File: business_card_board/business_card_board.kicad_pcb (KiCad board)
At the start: 2 copper layers, 85 x 54 mm, 23 parts, among them J1 PICKit3_Programmer, U1 PIC12F1822

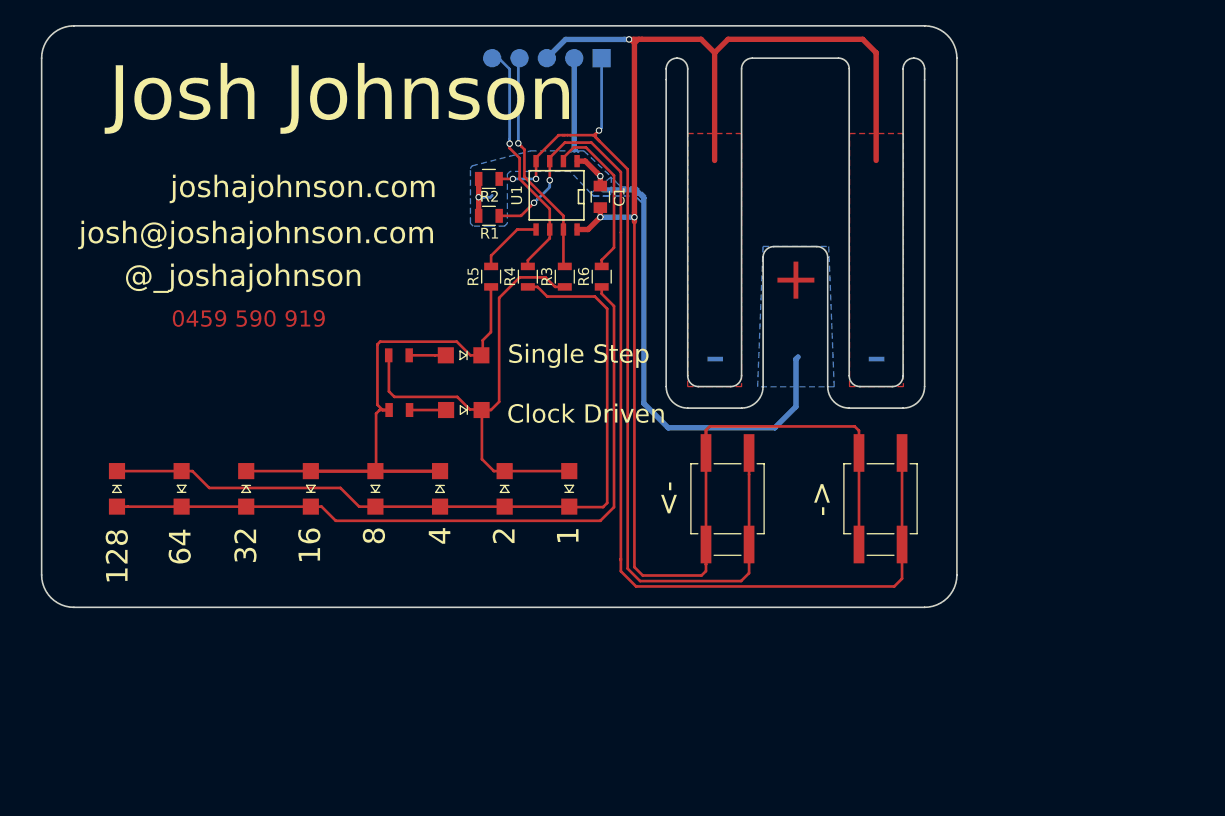
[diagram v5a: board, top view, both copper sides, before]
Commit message: board now at v1.1, improved mechanical layout + small routing changes
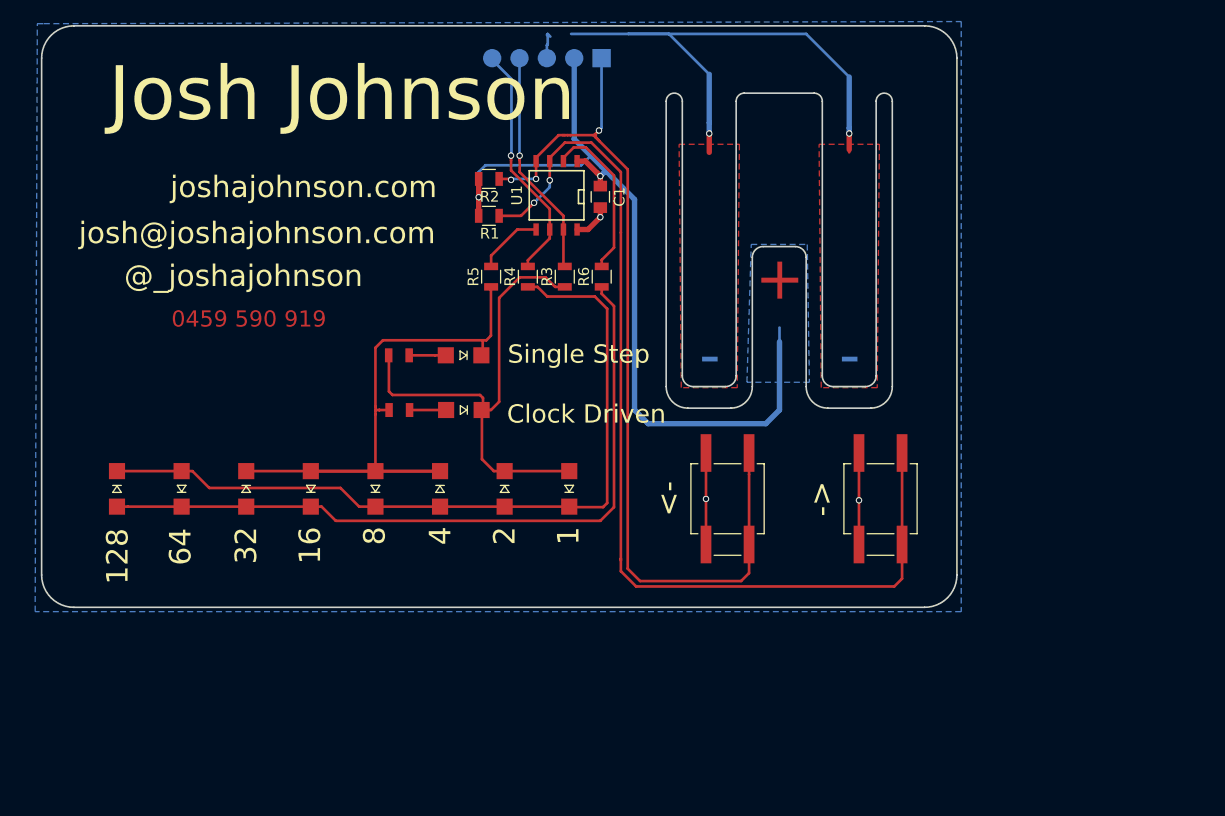
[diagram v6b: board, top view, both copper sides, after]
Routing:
- net GND: track 161.0 -> 75.0 mm, vias 3 -> 5
- net VCC: track 63.4 -> 85.0 mm
- net Net-(D1-Pad2): track 44.6 -> 45.3 mm
- net Net-(D3-Pad1): track 61.0 -> 60.4 mm
- added copper zone on B.Cu, net GND
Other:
- outline, holes or cut-outs redrawn

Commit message: more routing improvements
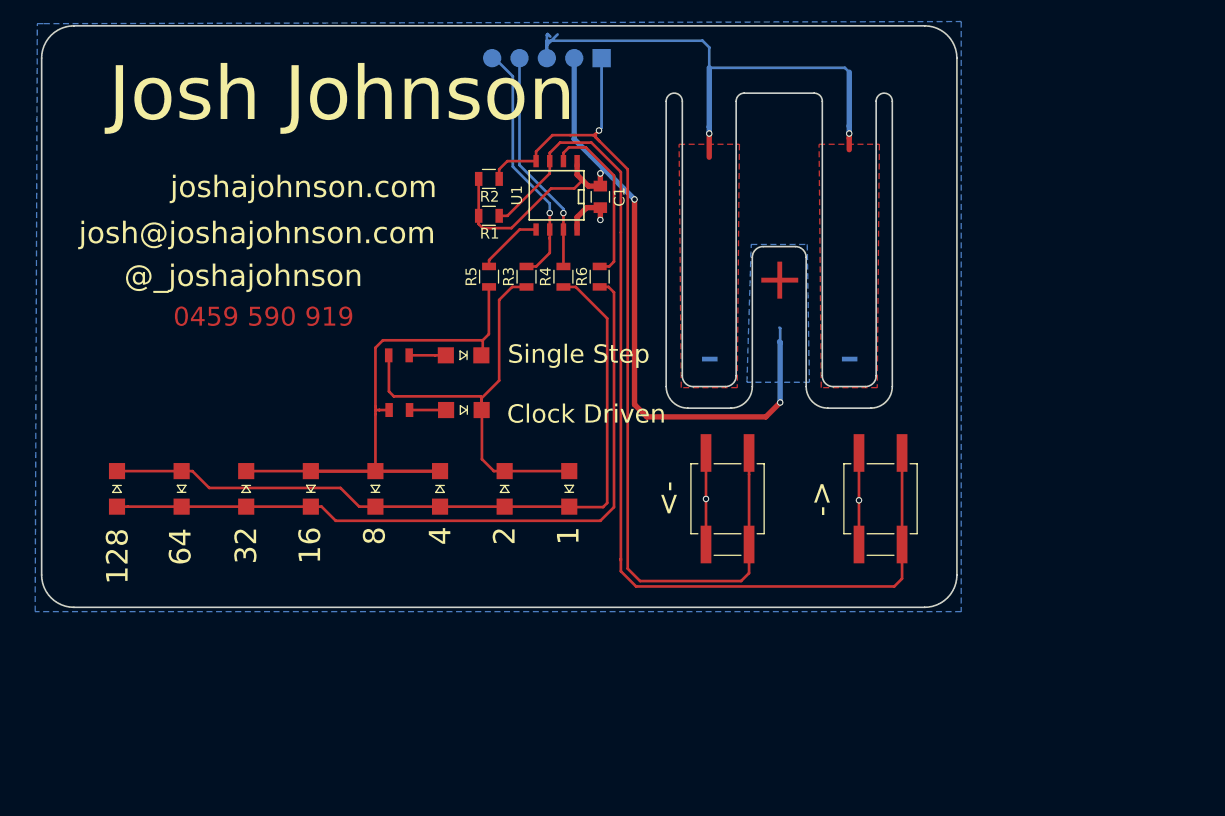
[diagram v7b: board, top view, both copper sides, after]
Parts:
- moved R3 3.56 mm to (105.0, 78.3)
- moved R4 3.30 mm to (108.5, 78.3)
- moved R5 0.19 mm to (101.6, 78.3)
- moved R6 0.19 mm to (111.8, 78.3)
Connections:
- R3 pad 2: ICSPDAT -> ICSPCLK
- R4 pad 2: ICSPCLK -> ICSPDAT
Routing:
- net Net-(D1-Pad2): track 45.3 -> 40.3 mm
- net Net-(D1-Pad1): track 73.3 -> 69.5 mm
- net VCC: track 85.0 -> 83.5 mm, vias 2 -> 3
- net RA5: track 15.4 -> 16.3 mm
- net ICSPCLK: track 22.4 -> 23.1 mm
- net Net-(D5-Pad1): track 68.4 -> 69.0 mm
- net Net-(R1-Pad2): track 92.7 -> 92.2 mm, vias 2 -> 0
- net VPP/~MCLR: track 85.0 -> 84.9 mm, vias 3 -> 1

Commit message: more routing changes
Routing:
- net VCC: track 83.5 -> 76.5 mm
- net GND: track 75.3 -> 71.2 mm
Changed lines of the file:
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@@
     (links 45)
     (no_connects 0)
-    (area 59.924999 54.924999 145.075001 109.075001)
+    (area 59.4 50.133333 145.400001 109.400001)
     (thickness 1.6)
     (drawings 49)
-    (tracks 205)
+    (tracks 198)
     (zones 0)
     (modules 23)
@@
     )
   )
+  (module business_card_footprints:Pin_Header_Straight_1x06_Pitch2.54mm_SMD (layer B.Cu)
+    (at 112 58 90)
+    (descr "Through hole straight pin header, 1x06, 2.54mm pitch, single row")
+    (tags "Through hole pin header THT 1x06 2.54mm single row")
+    (fp_text reference J1 (at 0 2.33 90) (layer B.Fab)
+      (effects (font (size 1 1) (thickness 0.15)) (justify mirror))
+    )
+    (fp_text value PICKit3_Programmer (at 0 -15.03 90) (layer B.Fab)
+      (effects (font (size 1 1) (thickness 0.15)) (justify mirror))
+    )
+    (fp_line (start -0.635 1.27) (end 1.27 1.27) (layer B.Fab) (width 0.1))
+    (fp_line (start 1.27 1.27) (end 1.27 -13.97) (layer B.Fab) (width 0.1))
+    (fp_line (start 1.27 -13.97) (end -1.27 -13.97) (layer B.Fab) (width 0.1))
+    (fp_line (start -1.27 -13.97) (end -1.27 0.635) (layer B.Fab) (width 0.1))
+    (fp_line (start -1.27 0.635) (end -0.635 1.27) (layer B.Fab) (width 0.1))
+    (fp_line (start -1.8 1.8) (end -1.8 -14.5) (layer B.CrtYd) (width 0.05))
+    (fp_line (start -1.8 -14.5) (end 1.8 -14.5) (layer B.CrtYd) (width 0.05))
+    (fp_line (start 1.8 -14.5) (end 1.8 1.8) (layer B.CrtYd) (width 0.05))
+    (fp_line (start 1.8 1.8) (end -1.8 1.8) (layer B.CrtYd) (width 0.05))
+    (fp_text user %R (at 0 -6.35 360) (layer B.Fab)
+      (effects (font (size 1 1) (thickness 0.15)) (justify mirror))
+    )
+    (pad 1 smd rect (at 0 0 90) (size 1.7 1.7) (layers B.Cu B.Paste B.Mask)
+      (net 9 VPP/~MCLR))
+    (pad 2 smd oval (at 0 -2.54 90) (size 1.7 1.7) (layers B.Cu B.Paste B.Mask)
+      (net 1 VCC))
+    (pad 3 smd oval (at 0 -5.08 90) (size 1.7 1.7) (layers B.Cu B.Paste B.Mask)
+      (net 2 GND))
+    (pad 4 smd oval (at 0 -7.62 90) (size 1.7 1.7) (layers B.Cu B.Paste B.Mask)
+      (net 10 ICSPDAT))
+    (pad 5 smd oval (at 0 -10.16 90) (size 1.7 1.7) (layers B.Cu B.Paste B.Mask)
+      (net 11 ICSPCLK))
+  )
   (module business_card_footprints:KSEK43GLFS_NoREFDES (layer F.Cu)
     (at 123.698 98.917 90)
@@
     (fp_line (start -3.1 3.25) (end -3.1 -3.25) (layer F.Fab) (width 0.1))
     (fp_circle (center 0 0) (end 1.25 0) (layer F.Fab) (width 0.1))
-    (fp_line (start -5.25 -1.25) (end -5.25 1.25) (layer F.SilkS) (width 0.12))
     (pad 2 smd rect (at 4.25 2 90) (size 3.5 1) (layers F.Cu F.Paste F.Mask)
       (net 9 VPP/~MCLR))
@@
     (fp_line (start -3.1 3.25) (end -3.1 -3.25) (layer F.Fab) (width 0.1))
     (fp_circle (center 0 0) (end 1.25 0) (layer F.Fab) (width 0.1))
-    (fp_line (start -5.25 -1.25) (end -5.25 1.25) (layer F.SilkS) (width 0.12))
     (pad 2 smd rect (at 4.25 2 90) (size 3.5 1) (layers F.Cu F.Paste F.Mask)
       (net 12 "Net-(R1-Pad2)"))
@@
       (rotate (xyz 0 0 0))
     )
-  )
-  (module business_card_footprints:Pin_Header_Straight_1x06_Pitch2.54mm_SMD (layer B.Cu)
-    (at 112 58 90)
-    (descr "Through hole straight pin header, 1x06, 2.54mm pitch, single row")
-    (tags "Through hole pin header THT 1x06 2.54mm single row")
-    (fp_text reference J1 (at 0 2.33 90) (layer B.Fab)
-      (effects (font (size 1 1) (thickness 0.15)) (justify mirror))
-    )
-    (fp_text value PICKit3_Programmer (at 0 -15.03 90) (layer B.Fab)
-      (effects (font (size 1 1) (thickness 0.15)) (justify mirror))
-    )
-    (fp_line (start -0.635 1.27) (end 1.27 1.27) (layer B.Fab) (width 0.1))
-    (fp_line (start 1.27 1.27) (end 1.27 -13.97) (layer B.Fab) (width 0.1))
-    (fp_line (start 1.27 -13.97) (end -1.27 -13.97) (layer B.Fab) (width 0.1))
-    (fp_line (start -1.27 -13.97) (end -1.27 0.635) (layer B.Fab) (width 0.1))
-    (fp_line (start -1.27 0.635) (end -0.635 1.27) (layer B.Fab) (width 0.1))
-    (fp_line (start -1.8 1.8) (end -1.8 -14.5) (layer B.CrtYd) (width 0.05))
-    (fp_line (start -1.8 -14.5) (end 1.8 -14.5) (layer B.CrtYd) (width 0.05))
-    (fp_line (start 1.8 -14.5) (end 1.8 1.8) (layer B.CrtYd) (width 0.05))
-    (fp_line (start 1.8 1.8) (end -1.8 1.8) (layer B.CrtYd) (width 0.05))
-    (fp_text user %R (at 0 -6.35 360) (layer B.Fab)
-      (effects (font (size 1 1) (thickness 0.15)) (justify mirror))
-    )
-    (pad 1 smd rect (at 0 0 90) (size 1.7 1.7) (layers B.Cu B.Paste B.Mask)
-      (net 9 VPP/~MCLR))
-    (pad 2 smd oval (at 0 -2.54 90) (size 1.7 1.7) (layers B.Cu B.Paste B.Mask)
-      (net 1 VCC))
-    (pad 3 smd oval (at 0 -5.08 90) (size 1.7 1.7) (layers B.Cu B.Paste B.Mask)
-      (net 2 GND))
-    (pad 4 smd oval (at 0 -7.62 90) (size 1.7 1.7) (layers B.Cu B.Paste B.Mask)
-      (net 10 ICSPDAT))
-    (pad 5 smd oval (at 0 -10.16 90) (size 1.7 1.7) (layers B.Cu B.Paste B.Mask)
-      (net 11 ICSPCLK))
   )
   (gr_line (start 131.75 61.25) (end 125.25 61.25) (layer Edge.Cuts) (width 0.15))
@@
   (via (at 128.5875 89.97949) (size 0.6) (drill 0.4) (layers F.Cu B.Cu) (net 1))
   (segment (start 128.5875 84.3915) (end 128.5875 89.999736) (width 0.5) (layer B.Cu) (net 1))
-  (segment (start 128.524 84.328) (end 128.5875 84.3915) (width 0.5) (layer B.Cu) (net 1))
-  (segment (start 128.524 83.024) (end 128.5875 83.0875) (width 0.25) (layer B.Cu) (net 1))
   (segment (start 128.5875 89.999736) (end 128.5875 89.97949) (width 0.25) (layer B.Cu) (net 1))
-  (segment (start 128.5875 83.0875) (end 128.5875 89.999736) (width 0.25) (layer B.Cu) (net 1))
   (segment (start 109.46 65.518) (end 110.998 67.056) (width 0.5) (layer B.Cu) (net 1))
   (segment (start 110.998 67.056) (end 112.014 68.072) (width 0.5) (layer B.Cu) (net 1))
@@
   (segment (start 106.92 58) (end 106.92 56.38) (width 0.25) (layer B.Cu) (net 2))
   (segment (start 106.92 58) (end 106.92 56.797919) (width 0.25) (layer B.Cu) (net 2))
-  (segment (start 106.92 56.797919) (end 107.917919 55.8) (width 0.25) (layer B.Cu) (net 2))
-  (segment (start 106.92 58) (end 106.92 55.84) (width 0.25) (layer B.Cu) (net 2))
-  (segment (start 107 55.76) (end 107.24 56) (width 0.25) (layer B.Cu) (net 2))
-  (segment (start 106.92 55.84) (end 107 55.76) (width 0.25) (layer B.Cu) (net 2))
   (via (at 135.906 99.06) (size 0.6) (drill 0.4) (layers F.Cu B.Cu) (net 2))
   (via (at 121.698 98.933) (size 0.6) (drill 0.4) (layers F.Cu B.Cu) (net 2))
@@
   (segment (start 107.188 74.7355) (end 107.188 73.914) (width 0.25) (layer F.Cu) (net 11))
   (segment (start 107.188 74.7395) (end 107.188 74.7355) (width 0.25) (layer F.Cu) (net 11))
-  (segment (start 107.188 67.564) (end 107.188 66.802) (width 0.25) (layer F.Cu) (net 12))
-  (segment (start 107.188 66.802) (end 108.146009 65.843991) (width 0.25) (layer F.Cu) (net 12))
-  (segment (start 108.146009 65.843991) (end 111.055991 65.843991) (width 0.25) (layer F.Cu) (net 12))
-  (segment (start 111.055991 65.843991) (end 113.791999 68.579999) (width 0.25) (layer F.Cu) (net 12))
+  (segment (start 107.188 67.564) (end 107.188 66.675) (width 0.25) (layer F.Cu) (net 12))
+  (segment (start 107.188 66.675) (end 108.077 65.786) (width 0.25) (layer F.Cu) (net 12))
+  (segment (start 108.077 65.786) (end 110.998 65.786) (width 0.25) (layer F.Cu) (net 12))
+  (segment (start 110.998 65.786) (end 113.791999 68.579999) (width 0.25) (layer F.Cu) (net 12))
   (segment (start 113.791999 68.579999) (end 113.791999 74.205414) (width 0.25) (layer F.Cu) (net 12))
   (segment (start 113.791999 74.205414) (end 113.791999 104.4956) (width 0.25) (layer F.Cu) (net 12))
@@
   (segment (start 101.5525 76.7555) (end 104.394 73.914) (width 0.25) (layer F.Cu) (net 13))
   (segment (start 104.394 73.914) (end 105.918 73.914) (width 0.25) (layer F.Cu) (net 13))
-  (segment (start 108.458 67.564) (end 108.458 66.802) (width 0.25) (layer F.Cu) (net 14))
-  (segment (start 108.965998 66.294002) (end 110.549004 66.294002) (width 0.25) (layer F.Cu) (net 14))
+  (segment (start 108.458 67.564) (end 108.458 66.675) (width 0.25) (layer F.Cu) (net 14))
+  (segment (start 108.458 66.675) (end 108.838998 66.294002) (width 0.25) (layer F.Cu) (net 14))
+  (segment (start 108.838998 66.294002) (end 110.549004 66.294002) (width 0.25) (layer F.Cu) (net 14))
+  (segment (start 112.7125 77.343) (end 111.8235 77.343) (width 0.25) (layer F.Cu) (net 14))
+  (segment (start 110.549004 66.294002) (end 113.157 68.901998) (width 0.25) (layer F.Cu) (net 14))
   (segment (start 113.157 68.901998) (end 113.157 76.8985) (width 0.25) (layer F.Cu) (net 14))
-  (segment (start 108.458 66.802) (end 108.965998 66.294002) (width 0.25) (layer F.Cu) (net 14))
-  (segment (start 110.549004 66.294002) (end 113.157 68.901998) (width 0.25) (layer F.Cu) (net 14))
   (segment (start 113.157 76.8985) (end 112.7125 77.343) (width 0.25) (layer F.Cu) (net 14))
-  (segment (start 112.7125 77.343) (end 111.8235 77.343) (width 0.25) (layer F.Cu) (net 14))
   (zone (net 0) (net_name "") (layer F.Mask) (hatch edge 0.508)
     (connect_pads (clearance 0.508))
